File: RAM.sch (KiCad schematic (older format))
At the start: 20 parts, among them J5 Conn_ARM_JTAG_SWD_20, SW4 SW_Push, U1 STM32MP151AAB3, U2 MT41K64M16TW-107_AAT_J_TR

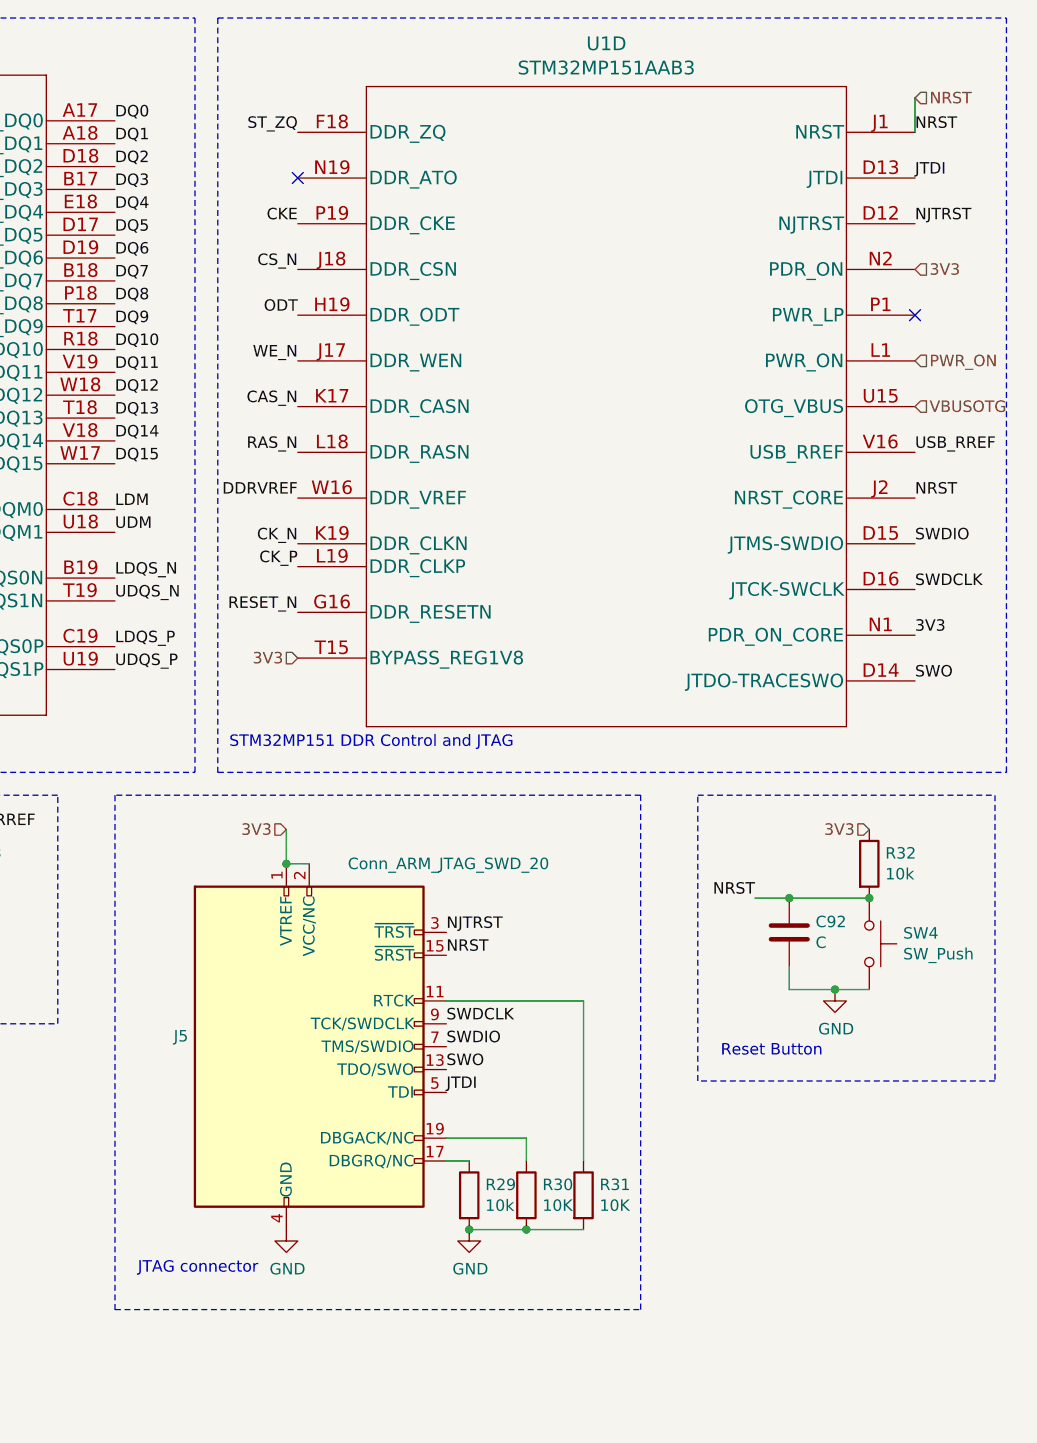
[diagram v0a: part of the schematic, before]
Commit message: Update jtag connector to swd
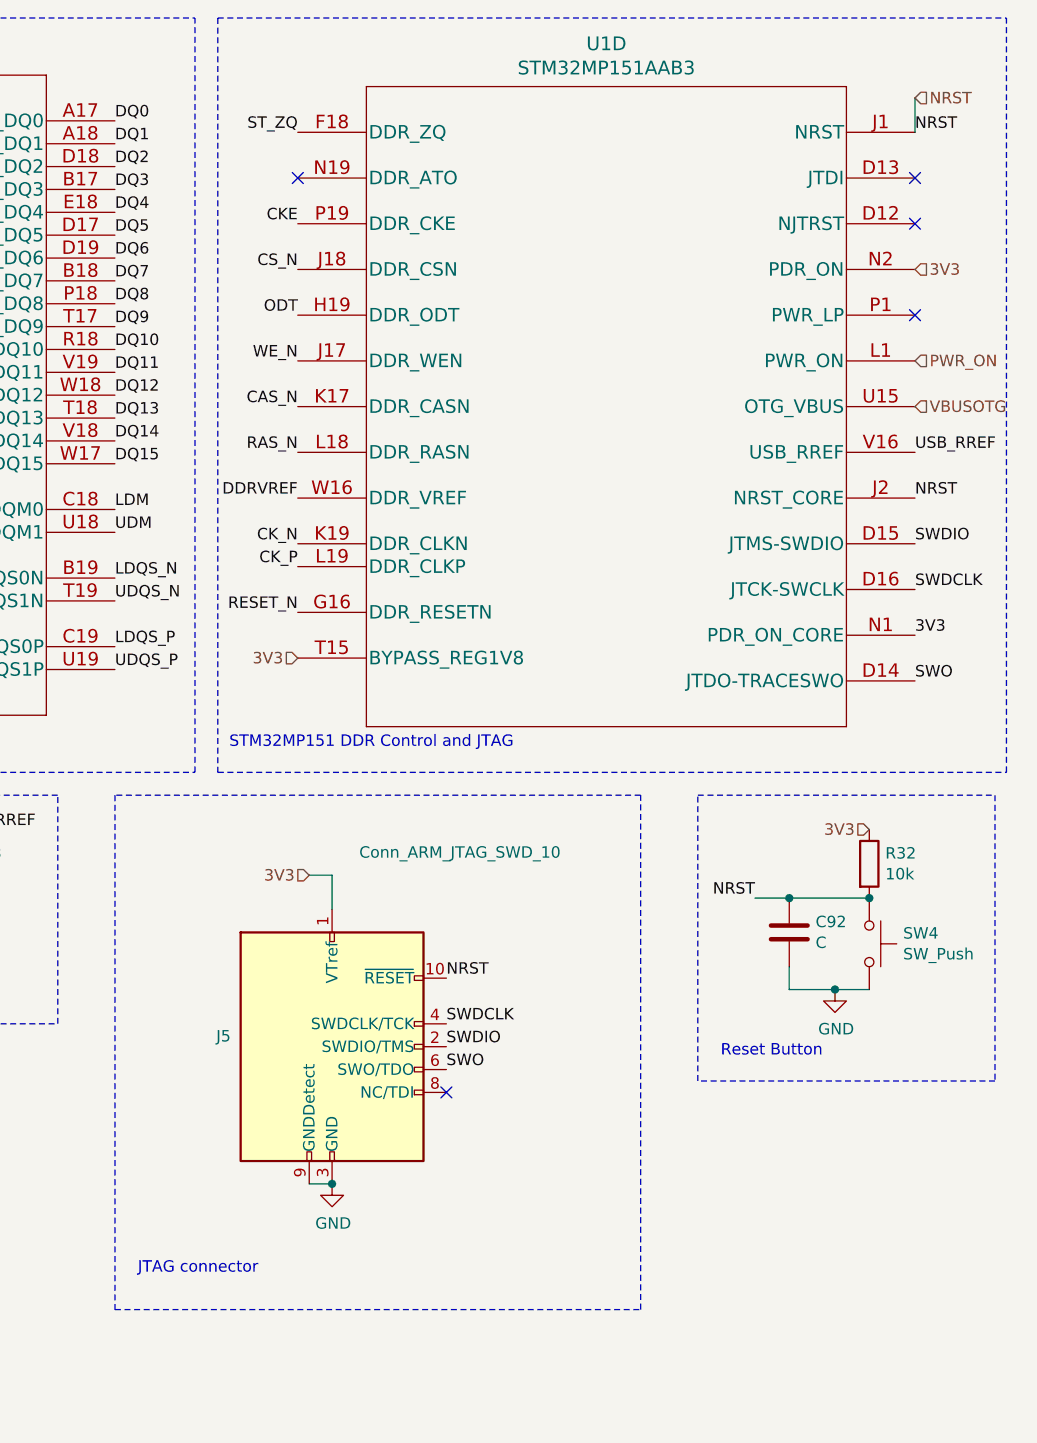
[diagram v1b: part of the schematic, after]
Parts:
- removed J5: Conn_ARM_JTAG_SWD_20, Connector_PinHeader_1.27mm:PinHeader_2x10_P1.27mm_Vertical, symbol Connector:Conn_ARM_JTAG_SWD_20
- removed R29: 10k, Resistor_SMD:R_0603_1608Metric_Pad1.05x0.95mm_HandSolder, symbol Device:R
- removed R30, R31: 10K, Resistor_SMD:R_0603_1608Metric_Pad1.05x0.95mm_HandSolder, symbol Device:R
- added J5: Conn_ARM_JTAG_SWD_10, Connector_PinHeader_1.27mm:PinHeader_2x05_P1.27mm_Vertical_SMD, symbol Connector:Conn_ARM_JTAG_SWD_10
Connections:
- net 3V3: now also J5.1 (VTref)
- net GND: now also J5.3 (GND), J5.5 (GND), J5.9 (GNDDetect)
- net NRST: now also J5.10 (~RESET~)
- net SWDCLK: now also J5.4 (SWDCLK/TCK)
- net SWDIO: now also J5.2 (SWDIO/TMS)
- net SWO: now also J5.6 (SWO/TDO)
- net JTDI: no longer names the net of U1.D13 (JTDI)
- net NJTRST: no longer names the net of U1.D12 (NJTRST)
- no-connect marks 8 -> 11
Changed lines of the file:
@@
 Connection ~ 10550 4500
-$Comp
-L Connector:Conn_ARM_JTAG_SWD_20 J5
-U 1 1 609DF11E
-P 8100 5150
-F 0 "J5" H 7571 5196 50  0000 R CNN
-F 1 "Conn_ARM_JTAG_SWD_20" H 9150 5950 50  0000 R CNN
-F 2 "Connector_PinHeader_1.27mm:PinHeader_2x10_P1.27mm_Vertical" H 8550 4100 50  0001 L TNN
-F 3 "http://infocenter.arm.com/help/topic/com.arm.doc.dui0499b/DUI0499B_system_design_reference.pdf" V 7750 3900 50  0001 C CNN
-	1    8100 5150
-	1    0    0    -1
-$EndComp
-Wire Wire Line
-	8000 4200 8000 4350
-Wire Wire Line
-	8000 4350 8100 4350
-Connection ~ 8000 4350
-Text Label 10750 1550 0    50   ~ 0
-NJTRST
-Text Label 8700 4650 0    50   ~ 0
-NJTRST
-Text Label 8700 5350 0    50   ~ 0
-JTDI
 $Comp
 L power:GND #PWR031
 U 1 1 60A09FC6
-P 8000 5950
-F 0 "#PWR031" H 8000 5700 50  0001 C CNN
-F 1 "GND" H 8005 5777 50  0000 C CNN
-F 2 "" H 8000 5950 50  0001 C CNN
-F 3 "" H 8000 5950 50  0001 C CNN
-	1    8000 5950
-	1    0    0    -1
-$EndComp
-$Comp
-L Device:R R30
-U 1 1 60A0BA82
-P 9050 5800
-F 0 "R30" H 9120 5846 50  0000 L CNN
-F 1 "10K" H 9120 5755 50  0000 L CNN
-F 2 "Resistor_SMD:R_0603_1608Metric_Pad1.05x0.95mm_HandSolder" V 8980 5800 50  0001 C CNN
-F 3 "~" H 9050 5800 50  0001 C CNN
-	1    9050 5800
-	1    0    0    -1
-$EndComp
-$Comp
-L Device:R R29
-U 1 1 60A0BE91
-P 8800 5800
-F 0 "R29" H 8870 5846 50  0000 L CNN
-F 1 "10k" H 8870 5755 50  0000 L CNN
-F 2 "Resistor_SMD:R_0603_1608Metric_Pad1.05x0.95mm_HandSolder" V 8730 5800 50  0001 C CNN
-F 3 "~" H 8800 5800 50  0001 C CNN
-	1    8800 5800
-	1    0    0    -1
-$EndComp
-Wire Wire Line
-	8700 5650 8800 5650
-Wire Wire Line
-	8700 5550 9050 5550
-Wire Wire Line
-	9050 5550 9050 5650
-$Comp
-L power:GND #PWR032
-U 1 1 60A0FFD6
-P 8800 5950
-F 0 "#PWR032" H 8800 5700 50  0001 C CNN
-F 1 "GND" H 8805 5777 50  0000 C CNN
-F 2 "" H 8800 5950 50  0001 C CNN
-F 3 "" H 8800 5950 50  0001 C CNN
-	1    8800 5950
-	1    0    0    -1
-$EndComp
-Wire Wire Line
-	8800 5950 9050 5950
-Connection ~ 8800 5950
-Text Label 10750 1350 0    50   ~ 0
-JTDI
-Text Label 8700 4750 0    50   ~ 0
+P 8200 5750
+F 0 "#PWR031" H 8200 5500 50  0001 C CNN
+F 1 "GND" H 8205 5577 50  0000 C CNN
+F 2 "" H 8200 5750 50  0001 C CNN
+F 3 "" H 8200 5750 50  0001 C CNN
+	1    8200 5750
+	1    0    0    -1
+$EndComp
+Text Label 8700 4850 0    50   ~ 0
 NRST
-$Comp
-L Device:R R31
-U 1 1 60A2D5B2
-P 9300 5800
-F 0 "R31" H 9370 5846 50  0000 L CNN
-F 1 "10K" H 9370 5755 50  0000 L CNN
-F 2 "Resistor_SMD:R_0603_1608Metric_Pad1.05x0.95mm_HandSolder" V 9230 5800 50  0001 C CNN
-F 3 "~" H 9300 5800 50  0001 C CNN
-	1    9300 5800
-	1    0    0    -1
-$EndComp
-Wire Wire Line
-	9050 5950 9300 5950
-Connection ~ 9050 5950
-Wire Wire Line
-	9300 5650 9300 4950
-Wire Wire Line
-	9300 4950 8700 4950
 Text Label 8700 5150 0    50   ~ 0
 SWDIO
@@
 Text Label 8050 2750 2    50   ~ 0
 DDRVREF
-Text HLabel 8000 4200 0    50   Input ~ 0
+Text HLabel 8100 4400 0    50   Input ~ 0
 3V3
 Text HLabel 10550 4200 0    50   Input ~ 0
@@
 NoConn ~ 4850 2600
 NoConn ~ 4850 2400
+$Comp
+L Connector:Conn_ARM_JTAG_SWD_10 J5
+U 1 1 609DA9D3
+P 8200 5150
+F 0 "J5" H 7757 5196 50  0000 R CNN
+F 1 "Conn_ARM_JTAG_SWD_10" H 9200 6000 50  0000 R CNN
+F 2 "Connector_PinHeader_1.27mm:PinHeader_2x05_P1.27mm_Vertical_SMD" H 8200 5150 50  0001 C CNN
+F 3 "http://infocenter.arm.com/help/topic/com.arm.doc.ddi0314h/DDI0314H_coresight_components_trm.pdf" V 7850 3900 50  0001 C CNN
+	1    8200 5150
+	1    0    0    -1
+$EndComp
+Wire Wire Line
+	8100 5750 8200 5750
+Connection ~ 8200 5750
+NoConn ~ 8700 5350
+NoConn ~ 10750 1550
+NoConn ~ 10750 1350
+Wire Wire Line
+	8100 4400 8200 4400
+Wire Wire Line
+	8200 4400 8200 4550
 $EndSCHEMATC

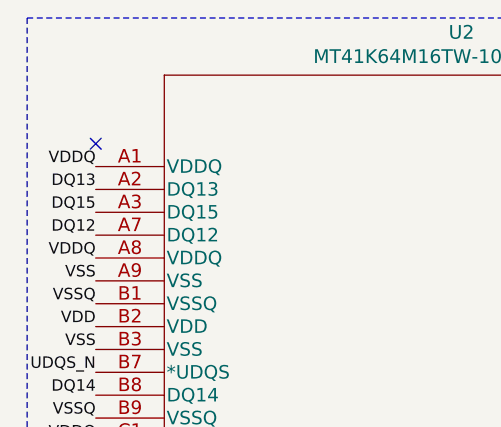
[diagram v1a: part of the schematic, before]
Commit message: Fix footprints
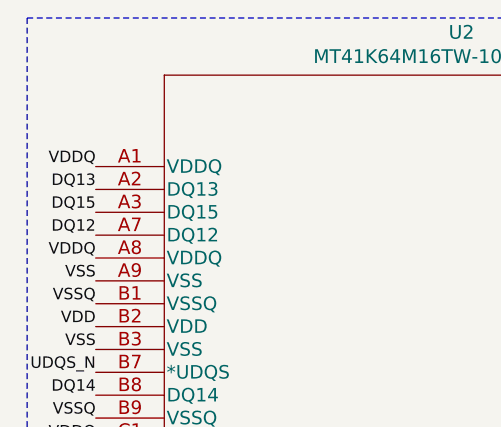
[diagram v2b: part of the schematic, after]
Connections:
- no-connect marks 11 -> 10
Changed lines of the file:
@@
 Text Label 1000 5500 2    50   ~ 0
 VREFDQ
-NoConn ~ 1000 1200
 Text Label 4200 1600 0    50   ~ 0
 RESET_N

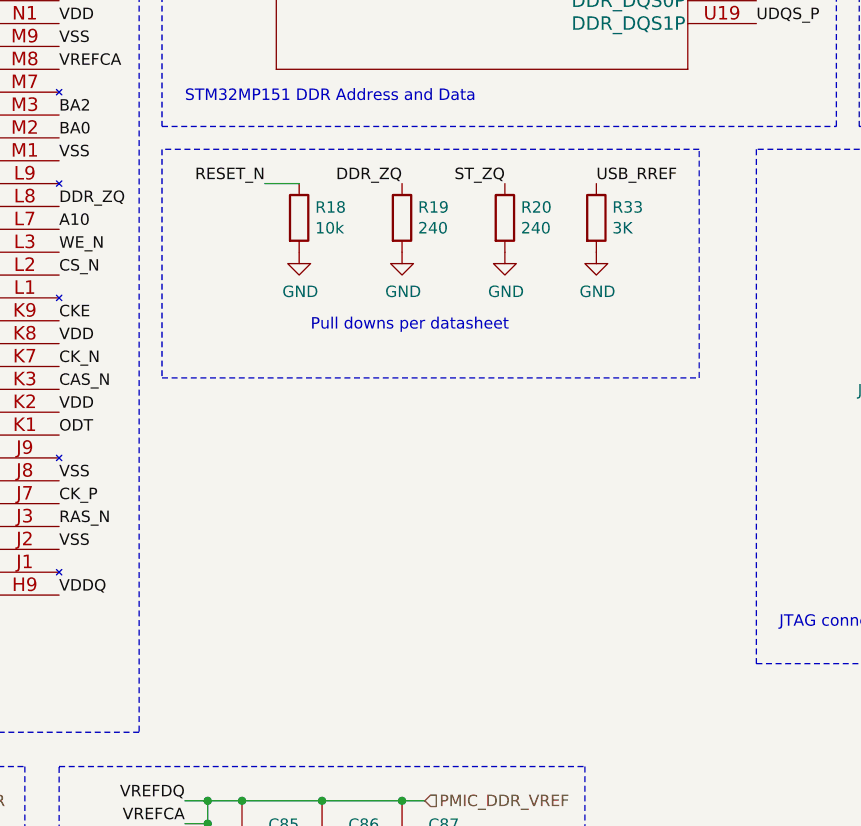
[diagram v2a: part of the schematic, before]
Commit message: Add mounting holes
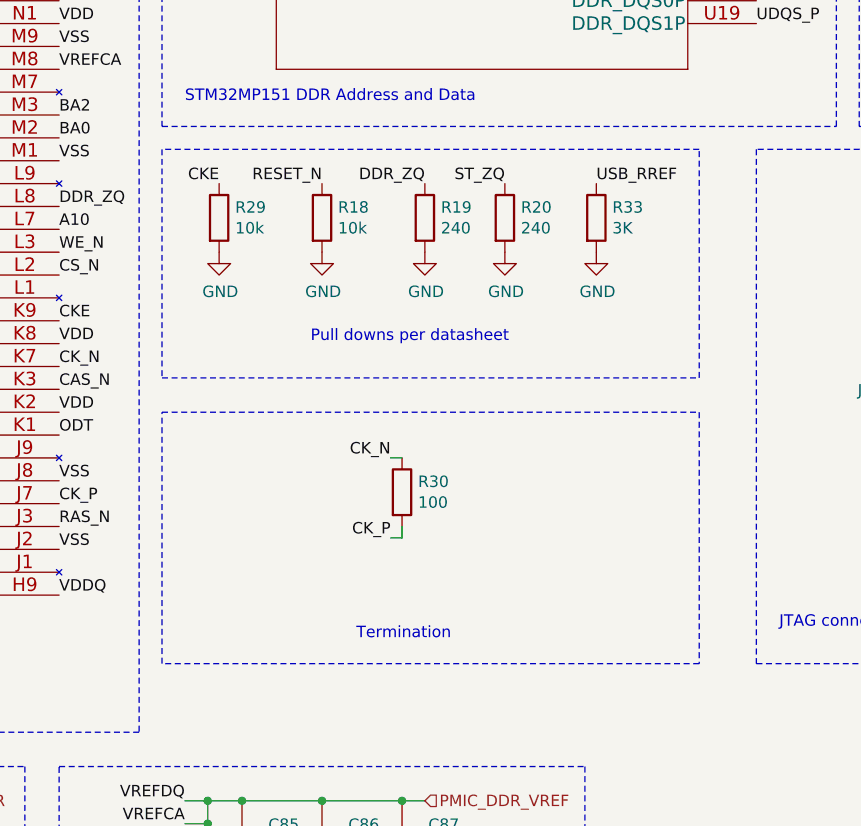
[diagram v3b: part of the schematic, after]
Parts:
- added R29: 10k, Resistor_SMD:R_0603_1608Metric_Pad1.05x0.95mm_HandSolder, symbol Device:R
- added R30: 100, symbol Device:R
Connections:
- net CKE: now also R29.1
- net CK_N: now also R30.1
- net CK_P: now also R30.2
- net GND: now also R29.2
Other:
- note added: "Termination\n"
- moved on the sheet: R18, R19
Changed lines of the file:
@@
 Text Label 4200 3700 0    50   ~ 0
 VREFCA
-Text Label 5100 4200 2    50   ~ 0
+Text Label 5350 4200 2    50   ~ 0
 RESET_N
 $Comp
 L Device:R R18
 U 1 1 6078BEF0
-P 5250 4350
-F 0 "R18" H 5320 4396 50  0000 L CNN
-F 1 "10k" H 5320 4305 50  0000 L CNN
-F 2 "Resistor_SMD:R_0603_1608Metric_Pad1.05x0.95mm_HandSolder" V 5180 4350 50  0001 C CNN
-F 3 "~" H 5250 4350 50  0001 C CNN
-	1    5250 4350
+P 5350 4350
+F 0 "R18" H 5420 4396 50  0000 L CNN
+F 1 "10k" H 5420 4305 50  0000 L CNN
+F 2 "Resistor_SMD:R_0603_1608Metric_Pad1.05x0.95mm_HandSolder" V 5280 4350 50  0001 C CNN
+F 3 "~" H 5350 4350 50  0001 C CNN
+	1    5350 4350
 	1    0    0    -1
 $EndComp
@@
 L power:GND #PWR0128
 U 1 1 6078C4BF
-P 5250 4500
-F 0 "#PWR0128" H 5250 4250 50  0001 C CNN
-F 1 "GND" H 5255 4327 50  0000 C CNN
-F 2 "" H 5250 4500 50  0001 C CNN
-F 3 "" H 5250 4500 50  0001 C CNN
-	1    5250 4500
-	1    0    0    -1
-$EndComp
-Wire Wire Line
-	5250 4200 5100 4200
+P 5350 4500
+F 0 "#PWR0128" H 5350 4250 50  0001 C CNN
+F 1 "GND" H 5355 4327 50  0000 C CNN
+F 2 "" H 5350 4500 50  0001 C CNN
+F 3 "" H 5350 4500 50  0001 C CNN
+	1    5350 4500
+	1    0    0    -1
+$EndComp
 Text Label 4750 7000 2    50   ~ 0
 VREFCA
@@
 Text Label 4200 4300 0    50   ~ 0
 DDR_ZQ
-Text Label 5700 4200 2    50   ~ 0
+Text Label 5800 4200 2    50   ~ 0
 DDR_ZQ
 Text Label 6150 4200 2    50   ~ 0
@@
 L Device:R R19
 U 1 1 6099FDB8
-P 5700 4350
-F 0 "R19" H 5770 4396 50  0000 L CNN
-F 1 "240" H 5770 4305 50  0000 L CNN
-F 2 "Resistor_SMD:R_0603_1608Metric" V 5630 4350 50  0001 C CNN
-F 3 "~" H 5700 4350 50  0001 C CNN
-	1    5700 4350
+P 5800 4350
+F 0 "R19" H 5870 4396 50  0000 L CNN
+F 1 "240" H 5870 4305 50  0000 L CNN
+F 2 "Resistor_SMD:R_0603_1608Metric" V 5730 4350 50  0001 C CNN
+F 3 "~" H 5800 4350 50  0001 C CNN
+	1    5800 4350
 	1    0    0    -1
 $EndComp
@@
 L power:GND #PWR0130
 U 1 1 609A2B11
-P 5700 4500
-F 0 "#PWR0130" H 5700 4250 50  0001 C CNN
-F 1 "GND" H 5705 4327 50  0000 C CNN
-F 2 "" H 5700 4500 50  0001 C CNN
-F 3 "" H 5700 4500 50  0001 C CNN
-	1    5700 4500
+P 5800 4500
+F 0 "#PWR0130" H 5800 4250 50  0001 C CNN
+F 1 "GND" H 5805 4327 50  0000 C CNN
+F 2 "" H 5800 4500 50  0001 C CNN
+F 3 "" H 5800 4500 50  0001 C CNN
+	1    5800 4500
 	1    0    0    -1
 $EndComp
@@
 Text Notes 4500 7350 0    50   ~ 0
 Decoupling Vref
-Text Notes 5300 4850 0    50   ~ 0
+Text Notes 5300 4900 0    50   ~ 0
 Pull downs per datasheet
 Text Notes 7350 6150 0    50   ~ 0
@@
 Wire Wire Line
 	8200 4400 8200 4550
+$Comp
+L Device:R R30
+U 1 1 60DBE80F
+P 5700 5550
+F 0 "R30" H 5770 5596 50  0000 L CNN
+F 1 "100" H 5770 5505 50  0000 L CNN
+F 2 "" V 5630 5550 50  0001 C CNN
+F 3 "~" H 5700 5550 50  0001 C CNN
+	1    5700 5550
+	1    0    0    -1
+$EndComp
+Text Label 5650 5400 2    50   ~ 0
+CK_N
+Text Label 5650 5750 2    50   ~ 0
+CK_P
+Wire Wire Line
+	5650 5400 5700 5400
+Wire Wire Line
+	5650 5750 5700 5750
+Wire Wire Line
+	5700 5750 5700 5700
+$Comp
+L Device:R R29
+U 1 1 60DF904C
+P 4900 4350
+F 0 "R29" H 4970 4396 50  0000 L CNN
+F 1 "10k" H 4970 4305 50  0000 L CNN
+F 2 "Resistor_SMD:R_0603_1608Metric_Pad1.05x0.95mm_HandSolder" V 4830 4350 50  0001 C CNN
+F 3 "~" H 4900 4350 50  0001 C CNN
+	1    4900 4350
+	1    0    0    -1
+$EndComp
+$Comp
+L power:GND #PWR0132
+U 1 1 60DF9052
+P 4900 4500
+F 0 "#PWR0132" H 4900 4250 50  0001 C CNN
+F 1 "GND" H 4905 4327 50  0000 C CNN
+F 2 "" H 4900 4500 50  0001 C CNN
+F 3 "" H 4900 4500 50  0001 C CNN
+	1    4900 4500
+	1    0    0    -1
+$EndComp
+Text Label 4900 4200 2    50   ~ 0
+CKE
+Wire Notes Line
+	4650 5200 7000 5200
+Wire Notes Line
+	7000 5200 7000 6300
+Wire Notes Line
+	7000 6300 4650 6300
+Wire Notes Line
+	4650 6300 4650 5200
+Text Notes 5500 6200 0    50   ~ 0
+Termination\n
 $EndSCHEMATC

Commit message: Add termination
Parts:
- R30: footprint (none) -> Resistor_SMD:R_0603_1608Metric_Pad1.05x0.95mm_HandSolder
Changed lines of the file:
@@
 F 0 "R30" H 5770 5596 50  0000 L CNN
 F 1 "100" H 5770 5505 50  0000 L CNN
-F 2 "" V 5630 5550 50  0001 C CNN
+F 2 "Resistor_SMD:R_0603_1608Metric_Pad1.05x0.95mm_HandSolder" V 5630 5550 50  0001 C CNN
 F 3 "~" H 5700 5550 50  0001 C CNN
 	1    5700 5550
